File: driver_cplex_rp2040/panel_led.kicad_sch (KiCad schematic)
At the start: 272 parts

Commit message: Added Charlieplexed version of rp2040 single pcb design.
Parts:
- R161: renamed from R102; value 180 -> 270
- R162: renamed from R103; value 180 -> 270
- R163: renamed from R104; value 180 -> 270
- R164: renamed from R105; value 180 -> 270
- R165: renamed from R106; value 180 -> 270
- R166: renamed from R107; value 180 -> 270
- R167: renamed from R108; value 180 -> 270
- R168: renamed from R109; value 180 -> 270
- R169: renamed from R110; value 180 -> 270
- R170: renamed from R111; value 180 -> 270
- R171: renamed from R112; value 180 -> 270
- R172: renamed from R113; value 180 -> 270
- R173: renamed from R114; value 180 -> 270
- R174: renamed from R115; value 180 -> 270
- R175: renamed from R116; value 180 -> 270
- R176: renamed from R117; value 180 -> 270
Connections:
- net COL_00: no longer names the net of R161.1
- net COL_01 renamed CP_5V_01
- net CP_5V_01: now also D1.2 (A), D114.2 (A), D130.2 (A), D146.2 (A), D162.2 (A), D17.1 (K), D178.2 (A), D18.1 (K), D19.1 (K), D194.2 (A), D20.1 (K), D21.1 (K), D210.2 (A), D22.1 (K), D226.2 (A), D23.1 (K), D24.1 (K), D242.2 (A), D25.1 (K), D26.1 (K), D27.1 (K), D28.1 (K), D29.1 (K), D30.1 (K), D31.1 (K), D32.1 (K), D34.2 (A), D50.2 (A), D66.2 (A), D82.2 (A), D98.2 (A), R162.2
- net COL_02 renamed CP_5V_02
- net CP_5V_02: now also D33.1 (K), D34.1 (K), D35.1 (K), D36.1 (K), D37.1 (K), D38.1 (K), D39.1 (K), D40.1 (K), D41.1 (K), D42.1 (K), D43.1 (K), D44.1 (K), D45.1 (K), D46.1 (K), D47.1 (K), D48.1 (K)
- net COL_03 renamed CP_5V_03
- net CP_5V_03: now also D100.2 (A), D116.2 (A), D132.2 (A), D148.2 (A), D164.2 (A), D180.2 (A), D196.2 (A), D212.2 (A), D228.2 (A), D244.2 (A), D49.1 (K), D50.1 (K), D51.1 (K), D52.1 (K), D53.1 (K), D54.1 (K), D55.1 (K), D56.1 (K), D57.1 (K), D58.1 (K), D59.1 (K), D60.1 (K), D61.1 (K), D62.1 (K), D63.1 (K), D64.1 (K), D84.2 (A)
- net COL_04: no longer names the net of R165.1
- net COL_05: no longer names the net of R166.1
- net COL_06: no longer names the net of R167.1
- net COL_07: no longer names the net of R168.1
- net COL_08: no longer names the net of R169.1
- net COL_09: no longer names the net of R170.1
- net COL_10: no longer names the net of R171.1
- net COL_11: no longer names the net of R172.1
- net COL_12: no longer names the net of R173.1
- net COL_13: no longer names the net of R174.1
- net COL_14: no longer names the net of R175.1
- net COL_15: no longer names the net of R176.1
- removed net ROW_00: D1.1 (K), D113.1 (K), D129.1 (K), D145.1 (K), D161.1 (K), D17.1 (K), D177.1 (K), D193.1 (K), D209.1 (K), D225.1 (K), D241.1 (K), D33.1 (K), D49.1 (K), D65.1 (K), D81.1 (K), D97.1 (K)
- removed net ROW_01: D114.1 (K), D130.1 (K), D146.1 (K), D162.1 (K), D178.1 (K), D18.1 (K), D194.1 (K), D2.1 (K), D210.1 (K), D226.1 (K), D242.1 (K), D34.1 (K), D50.1 (K), D66.1 (K), D82.1 (K), D98.1 (K)
- removed net ROW_02: D115.1 (K), D131.1 (K), D147.1 (K), D163.1 (K), D179.1 (K), D19.1 (K), D195.1 (K), D211.1 (K), D227.1 (K), D243.1 (K), D3.1 (K), D35.1 (K), D51.1 (K), D67.1 (K), D83.1 (K), D99.1 (K)
- removed net ROW_03: D100.1 (K), D116.1 (K), D132.1 (K), D148.1 (K), D164.1 (K), D180.1 (K), D196.1 (K), D20.1 (K), D212.1 (K), D228.1 (K), D244.1 (K), D36.1 (K), D4.1 (K), D52.1 (K), D68.1 (K), D84.1 (K)
- removed net ROW_04: D101.1 (K), D117.1 (K), D133.1 (K), D149.1 (K), D165.1 (K), D181.1 (K), D197.1 (K), D21.1 (K), D213.1 (K), D229.1 (K), D245.1 (K), D37.1 (K), D5.1 (K), D53.1 (K), D69.1 (K), D85.1 (K)
- removed net ROW_05: D102.1 (K), D118.1 (K), D134.1 (K), D150.1 (K), D166.1 (K), D182.1 (K), D198.1 (K), D214.1 (K), D22.1 (K), D230.1 (K), D246.1 (K), D38.1 (K), D54.1 (K), D6.1 (K), D70.1 (K), D86.1 (K)
- removed net ROW_06: D103.1 (K), D119.1 (K), D135.1 (K), D151.1 (K), D167.1 (K), D183.1 (K), D199.1 (K), D215.1 (K), D23.1 (K), D231.1 (K), D247.1 (K), D39.1 (K), D55.1 (K), D7.1 (K), D71.1 (K), D87.1 (K)
- removed net ROW_07: D104.1 (K), D120.1 (K), D136.1 (K), D152.1 (K), D168.1 (K), D184.1 (K), D200.1 (K), D216.1 (K), D232.1 (K), D24.1 (K), D248.1 (K), D40.1 (K), D56.1 (K), D72.1 (K), D8.1 (K), D88.1 (K)
- removed net ROW_08: D105.1 (K), D121.1 (K), D137.1 (K), D153.1 (K), D169.1 (K), D185.1 (K), D201.1 (K), D217.1 (K), D233.1 (K), D249.1 (K), D25.1 (K), D41.1 (K), D57.1 (K), D73.1 (K), D89.1 (K), D9.1 (K)
- removed net ROW_09: D10.1 (K), D106.1 (K), D122.1 (K), D138.1 (K), D154.1 (K), D170.1 (K), D186.1 (K), D202.1 (K), D218.1 (K), D234.1 (K), D250.1 (K), D26.1 (K), D42.1 (K), D58.1 (K), D74.1 (K), D90.1 (K)
- removed net ROW_10: D107.1 (K), D11.1 (K), D123.1 (K), D139.1 (K), D155.1 (K), D171.1 (K), D187.1 (K), D203.1 (K), D219.1 (K), D235.1 (K), D251.1 (K), D27.1 (K), D43.1 (K), D59.1 (K), D75.1 (K), D91.1 (K)
- removed net ROW_11: D108.1 (K), D12.1 (K), D124.1 (K), D140.1 (K), D156.1 (K), D172.1 (K), D188.1 (K), D204.1 (K), D220.1 (K), D236.1 (K), D252.1 (K), D28.1 (K), D44.1 (K), D60.1 (K), D76.1 (K), D92.1 (K)
- removed net ROW_12: D109.1 (K), D125.1 (K), D13.1 (K), D141.1 (K), D157.1 (K), D173.1 (K), D189.1 (K), D205.1 (K), D221.1 (K), D237.1 (K), D253.1 (K), D29.1 (K), D45.1 (K), D61.1 (K), D77.1 (K), D93.1 (K)
- removed net ROW_13: D110.1 (K), D126.1 (K), D14.1 (K), D142.1 (K), D158.1 (K), D174.1 (K), D190.1 (K), D206.1 (K), D222.1 (K), D238.1 (K), D254.1 (K), D30.1 (K), D46.1 (K), D62.1 (K), D78.1 (K), D94.1 (K)
- removed net ROW_14: D111.1 (K), D127.1 (K), D143.1 (K), D15.1 (K), D159.1 (K), D175.1 (K), D191.1 (K), D207.1 (K), D223.1 (K), D239.1 (K), D255.1 (K), D31.1 (K), D47.1 (K), D63.1 (K), D79.1 (K), D95.1 (K)
- removed net ROW_15: D112.1 (K), D128.1 (K), D144.1 (K), D16.1 (K), D160.1 (K), D176.1 (K), D192.1 (K), D208.1 (K), D224.1 (K), D240.1 (K), D256.1 (K), D32.1 (K), D48.1 (K), D64.1 (K), D80.1 (K), D96.1 (K)
- new net: D19.2 (A), D3.2 (A), D35.2 (A), D68.2 (A), R164.2
- new net: D115.2 (A), D131.2 (A), D147.2 (A), D163.2 (A), D179.2 (A), D18.2 (A), D195.2 (A), D2.2 (A), D211.2 (A), D227.2 (A), D243.2 (A), D51.2 (A), D67.2 (A), D83.2 (A), D99.2 (A), R163.2
- new net CP_5V_00: D1.1 (K), D10.1 (K), D11.1 (K), D113.2 (A), D12.1 (K), D129.2 (A), D13.1 (K), D14.1 (K), D145.2 (A), D15.1 (K), D16.1 (K), D161.2 (A), D17.2 (A), D177.2 (A), D193.2 (A), D2.1 (K), D209.2 (A), D225.2 (A), D241.2 (A), D3.1 (K), D33.2 (A), D4.1 (K), D49.2 (A), D5.1 (K), D6.1 (K), D65.2 (A), D7.1 (K), D8.1 (K), D81.2 (A), D9.1 (K), D97.2 (A)
- new net CP_5V_04: D101.2 (A), D117.2 (A), D133.2 (A), D149.2 (A), D165.2 (A), D181.2 (A), D197.2 (A), D20.2 (A), D213.2 (A), D229.2 (A), D245.2 (A), D36.2 (A), D52.2 (A), D65.1 (K), D66.1 (K), D67.1 (K), D68.1 (K), D69.1 (K), D70.1 (K), D71.1 (K), D72.1 (K), D73.1 (K), D74.1 (K), D75.1 (K), D76.1 (K), D77.1 (K), D78.1 (K), D79.1 (K), D80.1 (K), D85.2 (A)
- new net CP_5V_05: D102.2 (A), D118.2 (A), D134.2 (A), D150.2 (A), D166.2 (A), D182.2 (A), D198.2 (A), D21.2 (A), D214.2 (A), D230.2 (A), D246.2 (A), D37.2 (A), D53.2 (A), D69.2 (A), D81.1 (K), D82.1 (K), D83.1 (K), D84.1 (K), D85.1 (K), D86.1 (K), D87.1 (K), D88.1 (K), D89.1 (K), D90.1 (K), D91.1 (K), D92.1 (K), D93.1 (K), D94.1 (K), D95.1 (K), D96.1 (K)
- new net CP_5V_06: D100.1 (K), D101.1 (K), D102.1 (K), D103.1 (K), D104.1 (K), D105.1 (K), D106.1 (K), D107.1 (K), D108.1 (K), D109.1 (K), D110.1 (K), D111.1 (K), D112.1 (K), D119.2 (A), D135.2 (A), D151.2 (A), D167.2 (A), D183.2 (A), D199.2 (A), D215.2 (A), D22.2 (A), D231.2 (A), D247.2 (A), D38.2 (A), D54.2 (A), D70.2 (A), D86.2 (A), D97.1 (K), D98.1 (K), D99.1 (K)
- new net CP_5V_07: D103.2 (A), D113.1 (K), D114.1 (K), D115.1 (K), D116.1 (K), D117.1 (K), D118.1 (K), D119.1 (K), D120.1 (K), D121.1 (K), D122.1 (K), D123.1 (K), D124.1 (K), D125.1 (K), D126.1 (K), D127.1 (K), D128.1 (K), D136.2 (A), D152.2 (A), D168.2 (A), D184.2 (A), D200.2 (A), D216.2 (A), D23.2 (A), D232.2 (A), D248.2 (A), D39.2 (A), D55.2 (A), D71.2 (A), D87.2 (A)
- new net CP_5V_08: D104.2 (A), D120.2 (A), D129.1 (K), D130.1 (K), D131.1 (K), D132.1 (K), D133.1 (K), D134.1 (K), D135.1 (K), D136.1 (K), D137.1 (K), D138.1 (K), D139.1 (K), D140.1 (K), D141.1 (K), D142.1 (K), D143.1 (K), D144.1 (K), D153.2 (A), D169.2 (A), D185.2 (A), D201.2 (A), D217.2 (A), D233.2 (A), D24.2 (A), D249.2 (A), D40.2 (A), D56.2 (A), D72.2 (A), D88.2 (A)
- new net CP_5V_09: D105.2 (A), D121.2 (A), D137.2 (A), D145.1 (K), D146.1 (K), D147.1 (K), D148.1 (K), D149.1 (K), D150.1 (K), D151.1 (K), D152.1 (K), D153.1 (K), D154.1 (K), D155.1 (K), D156.1 (K), D157.1 (K), D158.1 (K), D159.1 (K), D160.1 (K), D170.2 (A), D186.2 (A), D202.2 (A), D218.2 (A), D234.2 (A), D25.2 (A), D250.2 (A), D41.2 (A), D57.2 (A), D73.2 (A), D89.2 (A)
- new net CP_5V_10: D106.2 (A), D122.2 (A), D138.2 (A), D154.2 (A), D161.1 (K), D162.1 (K), D163.1 (K), D164.1 (K), D165.1 (K), D166.1 (K), D167.1 (K), D168.1 (K), D169.1 (K), D170.1 (K), D171.1 (K), D172.1 (K), D173.1 (K), D174.1 (K), D175.1 (K), D176.1 (K), D187.2 (A), D203.2 (A), D219.2 (A), D235.2 (A), D251.2 (A), D26.2 (A), D42.2 (A), D58.2 (A), D74.2 (A), D90.2 (A)
- new net CP_5V_11: D107.2 (A), D123.2 (A), D139.2 (A), D155.2 (A), D171.2 (A), D177.1 (K), D178.1 (K), D179.1 (K), D180.1 (K), D181.1 (K), D182.1 (K), D183.1 (K), D184.1 (K), D185.1 (K), D186.1 (K), D187.1 (K), D188.1 (K), D189.1 (K), D190.1 (K), D191.1 (K), D192.1 (K), D204.2 (A), D220.2 (A), D236.2 (A), D252.2 (A), D27.2 (A), D43.2 (A), D59.2 (A), D75.2 (A), D91.2 (A)
- new net CP_5V_12: D108.2 (A), D124.2 (A), D140.2 (A), D156.2 (A), D172.2 (A), D188.2 (A), D193.1 (K), D194.1 (K), D195.1 (K), D196.1 (K), D197.1 (K), D198.1 (K), D199.1 (K), D200.1 (K), D201.1 (K), D202.1 (K), D203.1 (K), D204.1 (K), D205.1 (K), D206.1 (K), D207.1 (K), D208.1 (K), D221.2 (A), D237.2 (A), D253.2 (A), D28.2 (A), D44.2 (A), D60.2 (A), D76.2 (A), D92.2 (A)
- new net CP_5V_13: D109.2 (A), D125.2 (A), D141.2 (A), D157.2 (A), D173.2 (A), D189.2 (A), D205.2 (A), D209.1 (K), D210.1 (K), D211.1 (K), D212.1 (K), D213.1 (K), D214.1 (K), D215.1 (K), D216.1 (K), D217.1 (K), D218.1 (K), D219.1 (K), D220.1 (K), D221.1 (K), D222.1 (K), D223.1 (K), D224.1 (K), D238.2 (A), D254.2 (A), D29.2 (A), D45.2 (A), D61.2 (A), D77.2 (A), D93.2 (A)
- new net CP_5V_14: D110.2 (A), D126.2 (A), D142.2 (A), D158.2 (A), D174.2 (A), D190.2 (A), D206.2 (A), D222.2 (A), D225.1 (K), D226.1 (K), D227.1 (K), D228.1 (K), D229.1 (K), D230.1 (K), D231.1 (K), D232.1 (K), D233.1 (K), D234.1 (K), D235.1 (K), D236.1 (K), D237.1 (K), D238.1 (K), D239.1 (K), D240.1 (K), D255.2 (A), D30.2 (A), D46.2 (A), D62.2 (A), D78.2 (A), D94.2 (A)
- new net CP_5V_15: D111.2 (A), D127.2 (A), D143.2 (A), D159.2 (A), D175.2 (A), D191.2 (A), D207.2 (A), D223.2 (A), D239.2 (A), D241.1 (K), D242.1 (K), D243.1 (K), D244.1 (K), D245.1 (K), D246.1 (K), D247.1 (K), D248.1 (K), D249.1 (K), D250.1 (K), D251.1 (K), D252.1 (K), D253.1 (K), D254.1 (K), D255.1 (K), D256.1 (K), D31.2 (A), D47.2 (A), D63.2 (A), D79.2 (A), D95.2 (A)
- new net CP_5V_16: D112.2 (A), D128.2 (A), D144.2 (A), D160.2 (A), D176.2 (A), D192.2 (A), D208.2 (A), D224.2 (A), D240.2 (A), D256.2 (A), D32.2 (A), D48.2 (A), D64.2 (A), D80.2 (A), D96.2 (A)
- now unconnected: D10.2 (A), D11.2 (A), D12.2 (A), D13.2 (A), D14.2 (A), D15.2 (A), D16.2 (A), D4.2 (A), D5.2 (A), D6.2 (A), D7.2 (A), D8.2 (A), D9.2 (A), R161.2, R165.2, R166.2, R167.2, R168.2, R169.2, R170.2, R171.2, R172.2, R173.2, R174.2, R175.2, R176.2
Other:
- note added: "Not quite right!!!"
- moved on the sheet: D1, D10, D100, D101, D102, D103, D104, D105, D106, D107, D108, D109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

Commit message: Completed initial schematic of rp2040 design with charlieplexing.
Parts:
- added R177: 270, symbol Device:R
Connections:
- net CP_5V_00: now also R161.2; no longer D113.2 (A), D129.2 (A), D145.2 (A), D161.2 (A), D17.2 (A), D177.2 (A), D193.2 (A), D209.2 (A), D225.2 (A), D241.2 (A), D33.2 (A), D49.2 (A), D65.2 (A), D81.2 (A), D97.2 (A)
- net CP_5V_03: no longer D100.2 (A), D116.2 (A), D132.2 (A), D148.2 (A), D164.2 (A), D180.2 (A), D196.2 (A), D212.2 (A), D228.2 (A), D244.2 (A), D84.2 (A)
- net CP_5V_04: now also R165.1; no longer D101.2 (A), D117.2 (A), D133.2 (A), D149.2 (A), D165.2 (A), D181.2 (A), D197.2 (A), D20.2 (A), D213.2 (A), D229.2 (A), D245.2 (A), D36.2 (A), D52.2 (A), D85.2 (A)
- net CP_5V_05: now also R166.1; no longer D102.2 (A), D118.2 (A), D134.2 (A), D150.2 (A), D166.2 (A), D182.2 (A), D198.2 (A), D21.2 (A), D214.2 (A), D230.2 (A), D246.2 (A), D37.2 (A), D53.2 (A), D69.2 (A)
- net CP_5V_06: now also R167.1; no longer D119.2 (A), D135.2 (A), D151.2 (A), D167.2 (A), D183.2 (A), D199.2 (A), D215.2 (A), D22.2 (A), D231.2 (A), D247.2 (A), D38.2 (A), D54.2 (A), D70.2 (A), D86.2 (A)
- net CP_5V_07: now also R168.1; no longer D103.2 (A), D136.2 (A), D152.2 (A), D168.2 (A), D184.2 (A), D200.2 (A), D216.2 (A), D23.2 (A), D232.2 (A), D248.2 (A), D39.2 (A), D55.2 (A), D71.2 (A), D87.2 (A)
- net CP_5V_08: now also R169.1; no longer D104.2 (A), D120.2 (A), D153.2 (A), D169.2 (A), D185.2 (A), D201.2 (A), D217.2 (A), D233.2 (A), D24.2 (A), D249.2 (A), D40.2 (A), D56.2 (A), D72.2 (A), D88.2 (A)
- net CP_5V_09: now also R170.1; no longer D105.2 (A), D121.2 (A), D137.2 (A), D170.2 (A), D186.2 (A), D202.2 (A), D218.2 (A), D234.2 (A), D25.2 (A), D250.2 (A), D41.2 (A), D57.2 (A), D73.2 (A), D89.2 (A)
- net CP_5V_10: now also R171.1; no longer D106.2 (A), D122.2 (A), D138.2 (A), D154.2 (A), D187.2 (A), D203.2 (A), D219.2 (A), D235.2 (A), D251.2 (A), D26.2 (A), D42.2 (A), D58.2 (A), D74.2 (A), D90.2 (A)
- net CP_5V_11: now also R172.1; no longer D107.2 (A), D123.2 (A), D139.2 (A), D155.2 (A), D171.2 (A), D204.2 (A), D220.2 (A), D236.2 (A), D252.2 (A), D27.2 (A), D43.2 (A), D59.2 (A), D75.2 (A), D91.2 (A)
- net CP_5V_12: now also R173.1; no longer D108.2 (A), D124.2 (A), D140.2 (A), D156.2 (A), D172.2 (A), D188.2 (A), D221.2 (A), D237.2 (A), D253.2 (A), D28.2 (A), D44.2 (A), D60.2 (A), D76.2 (A), D92.2 (A)
- net CP_5V_13: now also R174.1; no longer D109.2 (A), D125.2 (A), D141.2 (A), D157.2 (A), D173.2 (A), D189.2 (A), D205.2 (A), D238.2 (A), D254.2 (A), D29.2 (A), D45.2 (A), D61.2 (A), D77.2 (A), D93.2 (A)
- net CP_5V_14: now also R175.1; no longer D110.2 (A), D126.2 (A), D142.2 (A), D158.2 (A), D174.2 (A), D190.2 (A), D206.2 (A), D222.2 (A), D255.2 (A), D30.2 (A), D46.2 (A), D62.2 (A), D78.2 (A), D94.2 (A)
- net CP_5V_15: now also R176.1; no longer D111.2 (A), D127.2 (A), D143.2 (A), D159.2 (A), D175.2 (A), D191.2 (A), D207.2 (A), D223.2 (A), D239.2 (A), D31.2 (A), D47.2 (A), D63.2 (A), D79.2 (A), D95.2 (A)
- net CP_5V_16: now also D16.2 (A), R177.1, R177.2
- net at D12.2 (A): now also D108.2 (A), D124.2 (A), D140.2 (A), D156.2 (A), D172.2 (A), D188.2 (A), D221.2 (A), D237.2 (A), D253.2 (A), D28.2 (A), D44.2 (A), D60.2 (A), D76.2 (A), D92.2 (A), R173.2
- net at D19.2 (A), D3.2 (A), D35.2 (A)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: now also D100.2 (A), D116.2 (A), D132.2 (A), D148.2 (A), D164.2 (A), D180.2 (A), D196.2 (A), D212.2 (A), D228.2 (A), D244.2 (A), D84.2 (A)
- net at R168.2: now also D103.2 (A), D136.2 (A), D152.2 (A), D168.2 (A), D184.2 (A), D200.2 (A), D216.2 (A), D23.2 (A), D232.2 (A), D248.2 (A), D39.2 (A), D55.2 (A), D7.2 (A), D71.2 (A), D87.2 (A)
- net at R175.2: now also D110.2 (A), D126.2 (A), D14.2 (A), D142.2 (A), D158.2 (A), D174.2 (A), D190.2 (A), D206.2 (A), D222.2 (A), D255.2 (A), D30.2 (A), D46.2 (A), D62.2 (A), D78.2 (A), D94.2 (A)
- net at R174.2: now also D109.2 (A), D125.2 (A), D13.2 (A), D141.2 (A), D157.2 (A), D173.2 (A), D189.2 (A), D205.2 (A), D238.2 (A), D254.2 (A), D29.2 (A), D45.2 (A), D61.2 (A), D77.2 (A), D93.2 (A)
- net at D15.2 (A): now also D111.2 (A), D127.2 (A), D143.2 (A), D159.2 (A), D175.2 (A), D191.2 (A), D207.2 (A), D223.2 (A), D239.2 (A), D31.2 (A), D47.2 (A), D63.2 (A), D79.2 (A), D95.2 (A), R176.2
- net at D6.2 (A): now also D119.2 (A), D135.2 (A), D151.2 (A), D167.2 (A), D183.2 (A), D199.2 (A), D215.2 (A), D22.2 (A), D231.2 (A), D247.2 (A), D38.2 (A), D54.2 (A), D70.2 (A), D86.2 (A), R167.2
- net at R171.2: now also D10.2 (A), D106.2 (A), D122.2 (A), D138.2 (A), D154.2 (A), D187.2 (A), D203.2 (A), D219.2 (A), D235.2 (A), D251.2 (A), D26.2 (A), D42.2 (A), D58.2 (A), D74.2 (A), D90.2 (A)
- net at R172.2: now also D107.2 (A), D11.2 (A), D123.2 (A), D139.2 (A), D155.2 (A), D171.2 (A), D204.2 (A), D220.2 (A), D236.2 (A), D252.2 (A), D27.2 (A), D43.2 (A), D59.2 (A), D75.2 (A), D91.2 (A)
- net at R166.2: now also D102.2 (A), D118.2 (A), D134.2 (A), D150.2 (A), D166.2 (A), D182.2 (A), D198.2 (A), D21.2 (A), D214.2 (A), D230.2 (A), D246.2 (A), D37.2 (A), D5.2 (A), D53.2 (A), D69.2 (A)
- net at D4.2 (A): now also D101.2 (A), D117.2 (A), D133.2 (A), D149.2 (A), D165.2 (A), D181.2 (A), D197.2 (A), D20.2 (A), D213.2 (A), D229.2 (A), D245.2 (A), D36.2 (A), D52.2 (A), D85.2 (A), R165.2
- net at D9.2 (A): now also D105.2 (A), D121.2 (A), D137.2 (A), D170.2 (A), D186.2 (A), D202.2 (A), D218.2 (A), D234.2 (A), D25.2 (A), D250.2 (A), D41.2 (A), D57.2 (A), D73.2 (A), D89.2 (A), R170.2
- net at R169.2: now also D104.2 (A), D120.2 (A), D153.2 (A), D169.2 (A), D185.2 (A), D201.2 (A), D217.2 (A), D233.2 (A), D24.2 (A), D249.2 (A), D40.2 (A), D56.2 (A), D72.2 (A), D8.2 (A), D88.2 (A)
- net at R161.1: now also D113.2 (A), D129.2 (A), D145.2 (A), D161.2 (A), D17.2 (A), D177.2 (A), D193.2 (A), D209.2 (A), D225.2 (A), D241.2 (A), D33.2 (A), D49.2 (A), D65.2 (A), D81.2 (A), D97.2 (A)
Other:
- note removed: "Not quite right!!!"
- moved on the sheet: D1, D10, D100, D101, D102, D103, D104, D105, D106, D107, D108, D109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

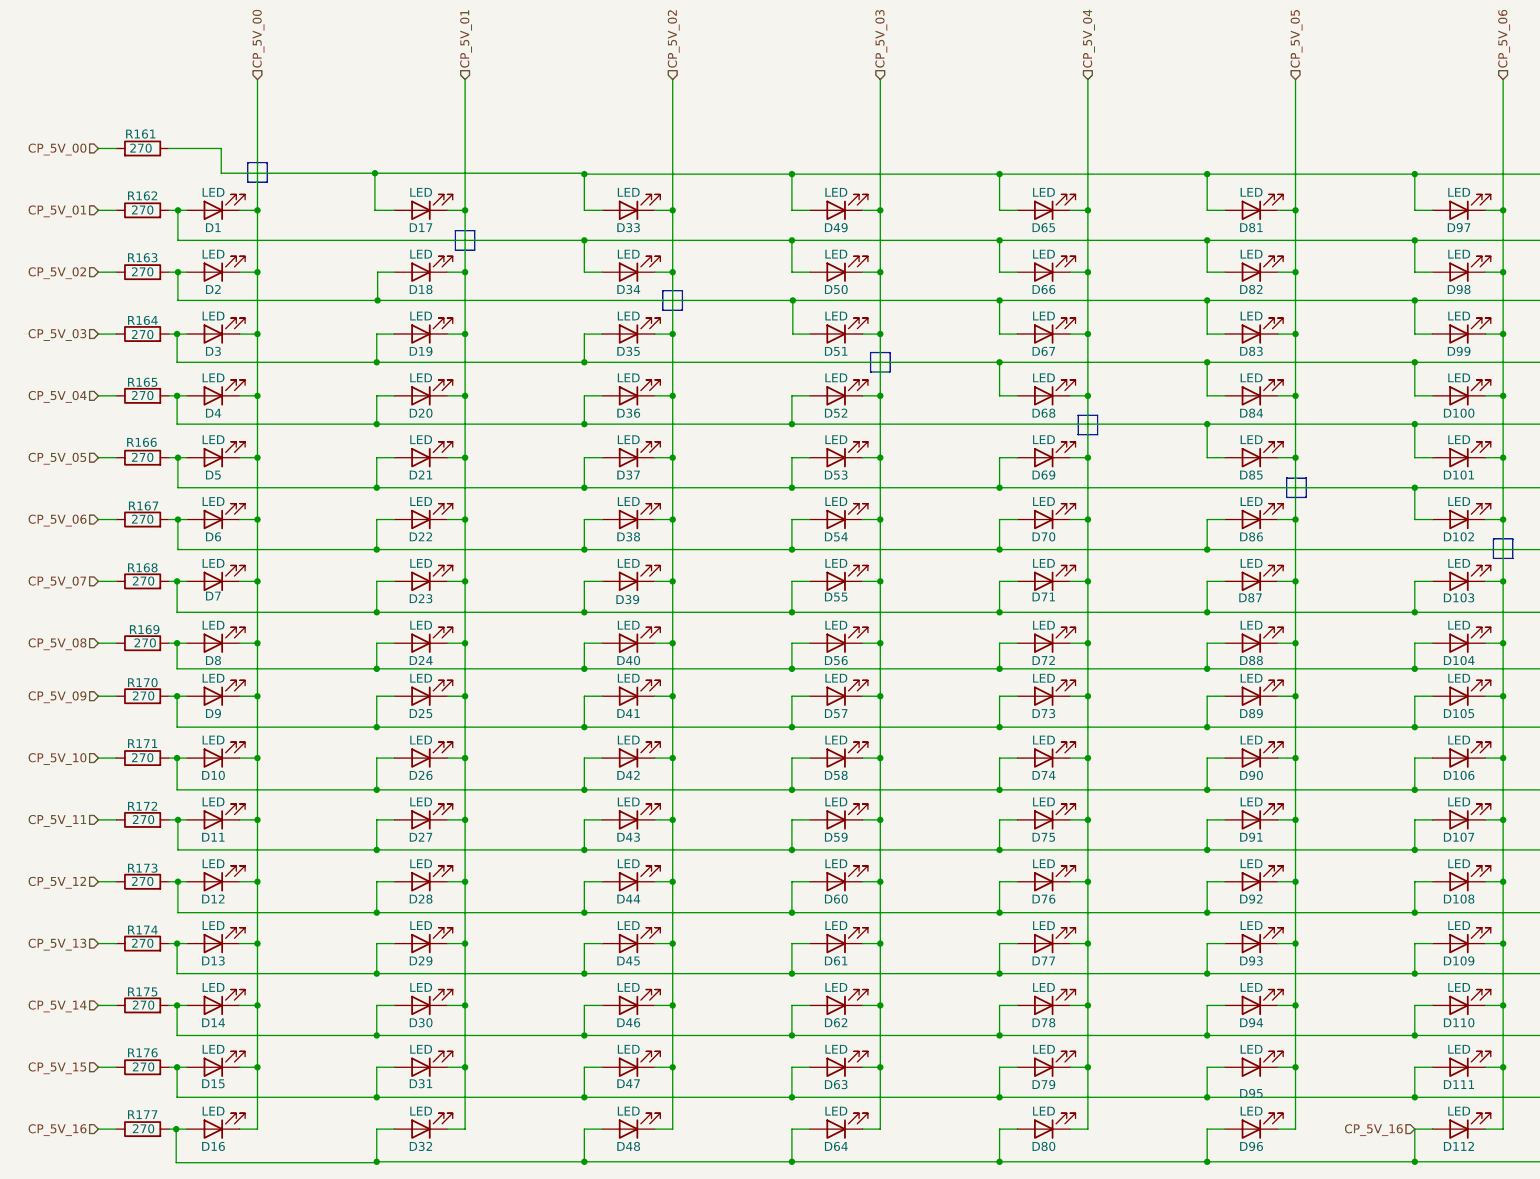
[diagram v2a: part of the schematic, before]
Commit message: Worked on footprint assignment for rp2040 single panel cplex design.
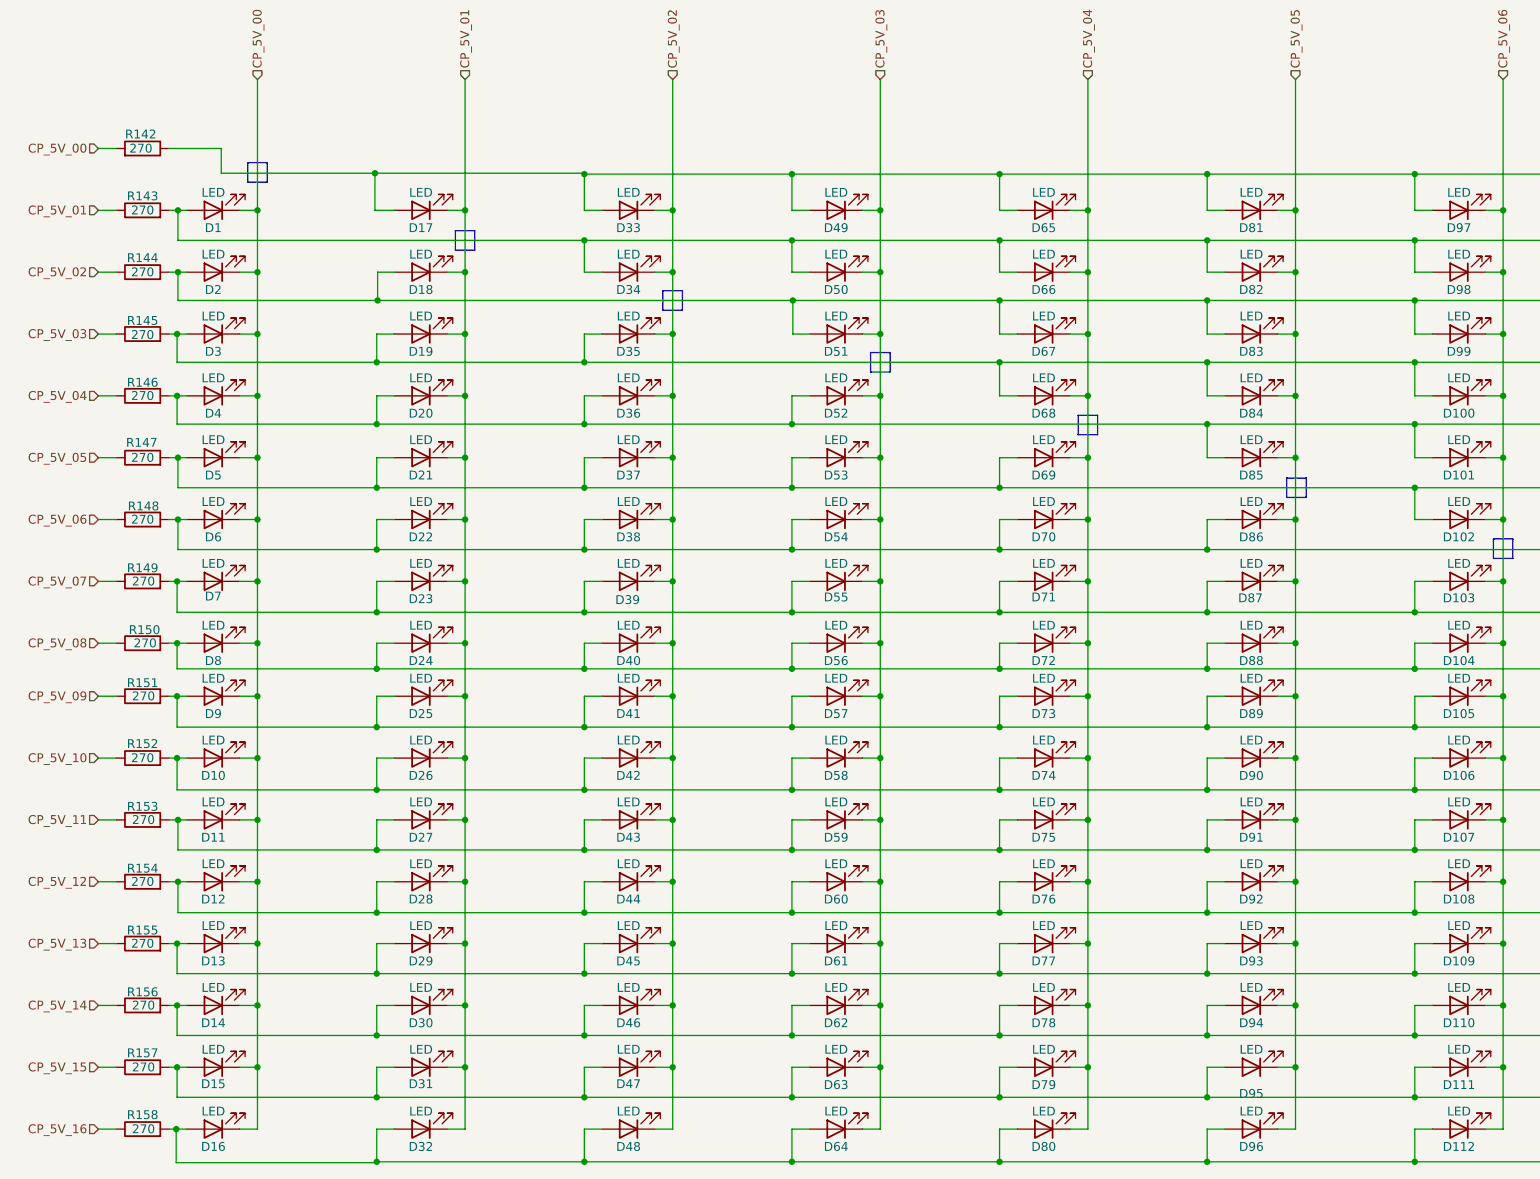
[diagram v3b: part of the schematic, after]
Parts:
- R142: renamed from R161; footprint (none) -> panel_custom:R_0201_0603Metric
- R143: renamed from R162; footprint (none) -> panel_custom:R_0201_0603Metric
- R144: renamed from R163; footprint (none) -> panel_custom:R_0201_0603Metric
- R145: renamed from R164; footprint (none) -> panel_custom:R_0201_0603Metric
- R146: renamed from R165; footprint (none) -> panel_custom:R_0201_0603Metric
- R147: renamed from R166; footprint (none) -> panel_custom:R_0201_0603Metric
- R148: renamed from R167; footprint (none) -> panel_custom:R_0201_0603Metric
- R149: renamed from R168; footprint (none) -> panel_custom:R_0201_0603Metric
- R150: renamed from R169; footprint (none) -> panel_custom:R_0201_0603Metric
- R151: renamed from R170; footprint (none) -> panel_custom:R_0201_0603Metric
- R152: renamed from R171; footprint (none) -> panel_custom:R_0201_0603Metric
- R153: renamed from R172; footprint (none) -> panel_custom:R_0201_0603Metric
- R154: renamed from R173; footprint (none) -> panel_custom:R_0201_0603Metric
- R155: renamed from R174; footprint (none) -> panel_custom:R_0201_0603Metric
- R156: renamed from R175; footprint (none) -> panel_custom:R_0201_0603Metric
- R157: renamed from R176; footprint (none) -> panel_custom:R_0201_0603Metric
- R158: renamed from R177; footprint (none) -> panel_custom:R_0201_0603Metric
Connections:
- net CP_5V_16: no longer D112.2 (A), D128.2 (A), D144.2 (A), D16.2 (A), D160.2 (A), D176.2 (A), D192.2 (A), D208.2 (A), D224.2 (A), D240.2 (A), D256.2 (A), D32.2 (A), D48.2 (A), D64.2 (A), D80.2 (A), D96.2 (A), R158.2
- new net: D112.2 (A), D128.2 (A), D144.2 (A), D16.2 (A), D160.2 (A), D176.2 (A), D192.2 (A), D208.2 (A), D224.2 (A), D240.2 (A), D256.2 (A), D32.2 (A), D48.2 (A), D64.2 (A), D80.2 (A), D96.2 (A), R158.2

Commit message: Worked on production files.
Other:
- note added: "LED C5160718"
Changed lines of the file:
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@@
     (fill (type color) (color 0 0 255 0.1))
+  )
+  (text "LED C5160718" (at 219.71 213.36 0)
+    (effects (font (size 2.54 2.54)) (justify left bottom))
   )
   (hierarchical_label "CP_5V_12" (shape input) (at 35.687 154.178 180) (fields_autoplaced)
